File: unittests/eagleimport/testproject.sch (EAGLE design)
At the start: 4 parts, among them U1 TESTDEVICE, U2 TESTDEVICE, U3 TESTDEVICE, U4 TESTDEVICE

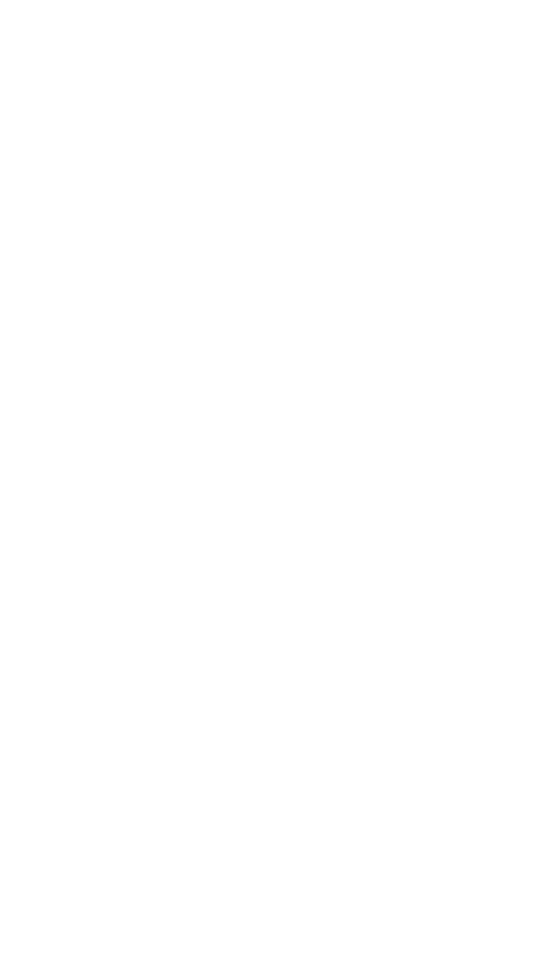
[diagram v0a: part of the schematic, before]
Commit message: Add buses to Eagle test project
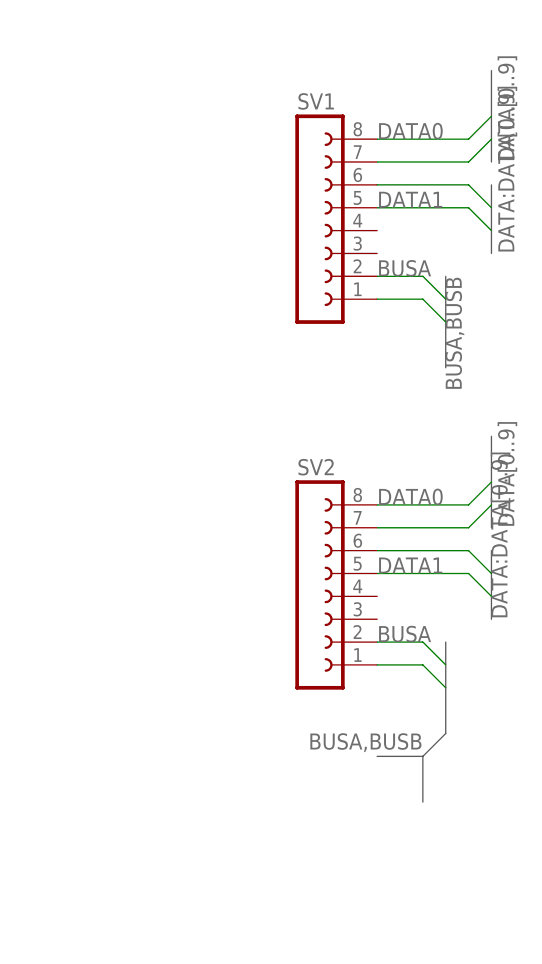
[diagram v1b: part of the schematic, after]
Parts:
- added SV1, SV2: (no value), con-lsta:FE08-1
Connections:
- new net BUSA: SV1.2, SV2.2
- new net BUSB: SV1.1, SV2.1
- new net DATA0: SV1.6, SV1.8, SV2.6, SV2.8
- new net DATA1: SV1.5, SV1.7, SV2.5, SV2.7
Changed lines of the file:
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@@
 <?xml version="1.0" encoding="utf-8"?>
 <!DOCTYPE eagle SYSTEM "eagle.dtd">
-<eagle version="9.6.0">
+<eagle version="9.6.2">
 <drawing>
 <settings>
@@
 <part name="P+1" library="supply1" library_urn="urn:adsk.eagle:library:371" deviceset="VCC" device=""/>
 <part name="P+2" library="supply1" library_urn="urn:adsk.eagle:library:371" deviceset="VCC" device=""/>
+<part name="SV1" library="con-lsta" library_urn="urn:adsk.eagle:library:161" deviceset="FE08-1" device="" package3d_urn="urn:adsk.eagle:package:8194/1"/>
+<part name="SV2" library="con-lsta" library_urn="urn:adsk.eagle:library:161" deviceset="FE08-1" device="" package3d_urn="urn:adsk.eagle:package:8194/1"/>
 </parts>
 <sheets>
@@
 <attribute name="VALUE" x="119.38" y="129.54" size="1.778" layer="96" rot="R90"/>
 </instance>
+<instance part="SV1" gate="G$1" x="226.06" y="154.94" smashed="yes">
+<attribute name="VALUE" x="224.79" y="142.24" size="1.778" layer="96"/>
+<attribute name="NAME" x="224.79" y="168.402" size="1.778" layer="95"/>
+</instance>
+<instance part="SV2" gate="G$1" x="226.06" y="114.3" smashed="yes">
+<attribute name="VALUE" x="224.79" y="101.6" size="1.778" layer="96"/>
+<attribute name="NAME" x="224.79" y="127.762" size="1.778" layer="95"/>
+</instance>
 </instances>
 <busses>
@@
 <wire x1="101.6" y1="99.06" x2="101.6" y2="134.62" width="0.762" layer="92"/>
 <label x="104.14" y="114.3" size="1.778" layer="95"/>
+</segment>
+</bus>
+<bus name="DATA[0..9]">
+<segment>
+<wire x1="246.38" y1="172.72" x2="246.38" y2="162.56" width="0.762" layer="92"/>
+<label x="248.92" y="162.56" size="1.778" layer="95" rot="R90"/>
+</segment>
+<segment>
+<wire x1="246.38" y1="132.08" x2="246.38" y2="121.92" width="0.762" layer="92"/>
+<label x="248.92" y="121.92" size="1.778" layer="95" rot="R90"/>
+</segment>
+</bus>
+<bus name="DATA:DATA[0..9]">
+<segment>
+<wire x1="246.38" y1="160.02" x2="246.38" y2="152.4" width="0.762" layer="92"/>
+<label x="248.92" y="152.4" size="1.778" layer="95" rot="R90"/>
+</segment>
+<segment>
+<wire x1="246.38" y1="119.38" x2="246.38" y2="111.76" width="0.762" layer="92"/>
+<label x="246.38" y="111.76" size="1.778" layer="95" rot="MR90"/>
+</segment>
+</bus>
+<bus name="BUSA,BUSB">
+<segment>
+<wire x1="241.3" y1="149.86" x2="241.3" y2="139.7" width="0.762" layer="92"/>
+<label x="241.3" y="149.86" size="1.778" layer="95" rot="R270"/>
+</segment>
+<segment>
+<wire x1="241.3" y1="109.22" x2="241.3" y2="99.06" width="0.762" layer="92"/>
+<label x="238.76" y="99.06" size="1.778" layer="95" rot="R180"/>
+<wire x1="241.3" y1="99.06" x2="238.76" y2="96.52" width="0.762" layer="92"/>
+<wire x1="238.76" y1="96.52" x2="233.68" y2="96.52" width="0.762" layer="92"/>
+<wire x1="238.76" y1="96.52" x2="238.76" y2="91.44" width="0.762" layer="92"/>
 </segment>
 </bus>
@@
 <label x="132.08" y="55.88" size="1.778" layer="95" rot="MR270" xref="yes"/>
 <label x="137.16" y="55.88" size="1.778" layer="95" rot="MR270" xref="yes"/>
+</segment>
+</net>
+<net name="DATA0" class="0">
+<segment>
+<pinref part="SV1" gate="G$1" pin="8"/>
+<wire x1="233.68" y1="165.1" x2="243.84" y2="165.1" width="0.1524" layer="91"/>
+<wire x1="243.84" y1="165.1" x2="246.38" y2="167.64" width="0.1524" layer="91"/>
+<label x="233.68" y="165.1" size="1.778" layer="95"/>
+</segment>
+<segment>
+<pinref part="SV1" gate="G$1" pin="6"/>
+<wire x1="233.68" y1="160.02" x2="243.84" y2="160.02" width="0.1524" layer="91"/>
+<wire x1="243.84" y1="160.02" x2="246.38" y2="157.48" width="0.1524" layer="91"/>
+</segment>
+<segment>
+<pinref part="SV2" gate="G$1" pin="8"/>
+<wire x1="233.68" y1="124.46" x2="243.84" y2="124.46" width="0.1524" layer="91"/>
+<wire x1="243.84" y1="124.46" x2="246.38" y2="127" width="0.1524" layer="91"/>
+<label x="233.68" y="124.46" size="1.778" layer="95"/>
+</segment>
+<segment>
+<pinref part="SV2" gate="G$1" pin="6"/>
+<wire x1="233.68" y1="119.38" x2="243.84" y2="119.38" width="0.1524" layer="91"/>
+<wire x1="243.84" y1="119.38" x2="246.38" y2="116.84" width="0.1524" layer="91"/>
+</segment>
+</net>
+<net name="DATA1" class="0">
+<segment>
+<pinref part="SV1" gate="G$1" pin="7"/>
+<wire x1="233.68" y1="162.56" x2="243.84" y2="162.56" width="0.1524" layer="91"/>
+<wire x1="243.84" y1="162.56" x2="246.38" y2="165.1" width="0.1524" layer="91"/>
+</segment>
+<segment>
+<pinref part="SV1" gate="G$1" pin="5"/>
+<wire x1="233.68" y1="157.48" x2="243.84" y2="157.48" width="0.1524" layer="91"/>
+<wire x1="243.84" y1="157.48" x2="246.38" y2="154.94" width="0.1524" layer="91"/>
+<label x="233.68" y="157.48" size="1.778" layer="95"/>
+</segment>
+<segment>
+<pinref part="SV2" gate="G$1" pin="7"/>
+<wire x1="233.68" y1="121.92" x2="243.84" y2="121.92" width="0.1524" layer="91"/>
+<wire x1="243.84" y1="121.92" x2="246.38" y2="124.46" width="0.1524" layer="91"/>
+</segment>
+<segment>
+<pinref part="SV2" gate="G$1" pin="5"/>
+<wire x1="233.68" y1="116.84" x2="243.84" y2="116.84" width="0.1524" layer="91"/>
+<wire x1="243.84" y1="116.84" x2="246.38" y2="114.3" width="0.1524" layer="91"/>
+<label x="233.68" y="116.84" size="1.778" layer="95"/>
+</segment>
+</net>
+<net name="BUSB" class="0">
+<segment>
+<pinref part="SV1" gate="G$1" pin="1"/>
+<wire x1="233.68" y1="147.32" x2="238.76" y2="147.32" width="0.1524" layer="91"/>
+<wire x1="238.76" y1="147.32" x2="241.3" y2="144.78" width="0.1524" layer="91"/>
+</segment>
+<segment>
+<pinref part="SV2" gate="G$1" pin="1"/>
+<wire x1="233.68" y1="106.68" x2="238.76" y2="106.68" width="0.1524" layer="91"/>
+<wire x1="238.76" y1="106.68" x2="241.3" y2="104.14" width="0.1524" layer="91"/>
+</segment>
+</net>
+<net name="BUSA" class="0">
+<segment>
+<pinref part="SV1" gate="G$1" pin="2"/>
+<wire x1="233.68" y1="149.86" x2="238.76" y2="149.86" width="0.1524" layer="91"/>
+<wire x1="238.76" y1="149.86" x2="241.3" y2="147.32" width="0.1524" layer="91"/>
+<label x="233.68" y="149.86" size="1.778" layer="95"/>
+</segment>
+<segment>
+<pinref part="SV2" gate="G$1" pin="2"/>
+<wire x1="233.68" y1="109.22" x2="238.76" y2="109.22" width="0.1524" layer="91"/>
+<wire x1="238.76" y1="109.22" x2="241.3" y2="106.68" width="0.1524" layer="91"/>
+<label x="233.68" y="109.22" size="1.778" layer="95"/>
 </segment>
 </net>
@@
 will not be understood (or retained) with this version.
 </note>
+<note version="8.3" severity="warning">
+Since Version 8.3, EAGLE supports the association of 3D packages
+with devices in libraries, schematics, and board files. Those 3D
+packages will not be understood (or retained) with this version.
+</note>
 <note version="9.0" severity="warning">
